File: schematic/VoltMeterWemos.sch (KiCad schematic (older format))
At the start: 22 parts, among them J1 TEST_1P, Q1 BS250, Q2 2N7000, SW1 SW_SPST, SW2 SW_SPST, U1 WeMosD1MiniPro

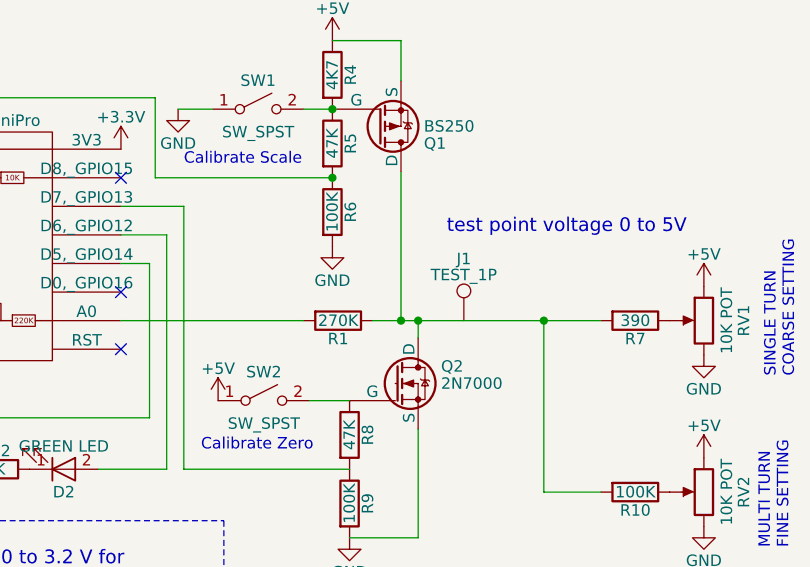
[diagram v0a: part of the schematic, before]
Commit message: capacitor added to A0
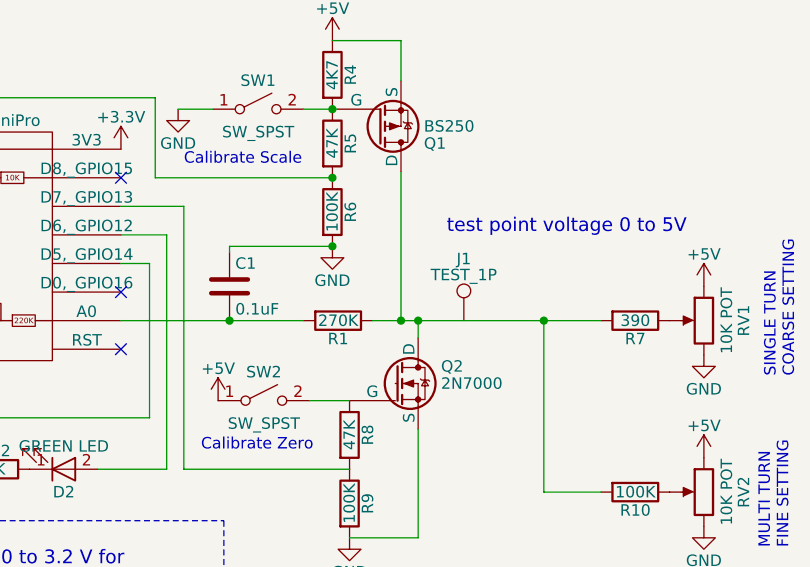
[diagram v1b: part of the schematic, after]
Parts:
- added C1: 0.1uF, symbol C
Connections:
- net GND: now also C1.1
- net at R1.2, U1.10 (A0): now also C1.2
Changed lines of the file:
@@
 NoConn ~ 4250 3450
 Wire Wire Line
-	5350 3325 5475 3325
-Wire Wire Line
-	5475 3325 5550 3325
-Wire Wire Line
-	5550 3325 6100 3325
-Wire Wire Line
-	6100 3325 6350 3325
+	5350 3325 6350 3325
 Text Notes 5675 2950 0    60   ~ 0
 test point voltage 0 to 5V
@@
 	1    0    0    -1
 $EndComp
+$Comp
+L C C1
+U 1 1 5A00E659
+P 4725 3175
+F 0 "C1" H 4750 3275 50  0000 L CNN
+F 1 "0.1uF" H 4750 3075 50  0000 L CNN
+F 2 "" H 4763 3025 50  0001 C CNN
+F 3 "" H 4725 3175 50  0001 C CNN
+	1    4725 3175
+	1    0    0    -1
+$EndComp
+Wire Wire Line
+	5175 3000 4725 3000
+Wire Wire Line
+	4725 3000 4725 3025
+Connection ~ 5175 3000
+Connection ~ 4725 3325
 $EndSCHEMATC

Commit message: lots of software and schematic updates, see diary for details. Moved results files to a private area since they are not of general interest.
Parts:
- Q1: value BS250 -> IR4905
- Q2: value 2N7000 -> IRFZ44N
- R7: value 390 -> 1000
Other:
- note added: "MULTI TURN\nCOARSE SETTING"
- note added: "SINGLE TURN\nFINE SETTING"
- note removed: "MULTI TURN\nFINE SETTING"
- note removed: "SINGLE TURN\nCOARSE SETTING"
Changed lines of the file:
@@
 P 5450 3600
 F 0 "Q2" H 5650 3675 50  0000 L CNN
-F 1 "2N7000" H 5650 3600 50  0000 L CNN
+F 1 "IRFZ44N" H 5650 3600 50  0000 L CNN
 F 2 "TO_SOT_Packages_THT:TO-92_Molded_Narrow" H 5650 3525 50  0001 L CIN
 F 3 "" H 5450 3600 50  0001 L CNN
@@
 P 5375 2475
 F 0 "Q1" H 5575 2550 50  0000 L CNN
-F 1 "BS250" H 5575 2475 50  0000 L CNN
+F 1 "IR4905" H 5575 2475 50  0000 L CNN
 F 2 "TO_SOT_Packages_THT:TO-92_Molded_Narrow" H 5575 2400 50  0001 L CIN
 F 3 "" H 5375 2475 50  0001 L CNN
@@
 P 6500 3325
 F 0 "R7" V 6580 3325 50  0000 C CNN
-F 1 "390" V 6500 3325 50  0000 C CNN
+F 1 "1000" V 6500 3325 50  0000 C CNN
 F 2 "" V 6430 3325 50  0001 C CNN
 F 3 "" H 6500 3325 50  0001 C CNN
@@
 Connection ~ 6100 3325
 Text Notes 7200 3575 1    50   ~ 0
-SINGLE TURN\nCOARSE SETTING
+MULTI TURN\nCOARSE SETTING
 Text Notes 7175 4325 1    50   ~ 0
-MULTI TURN\nFINE SETTING
+SINGLE TURN\nFINE SETTING
 Text Notes 4600 3900 0    50   ~ 0
 Calibrate Zero

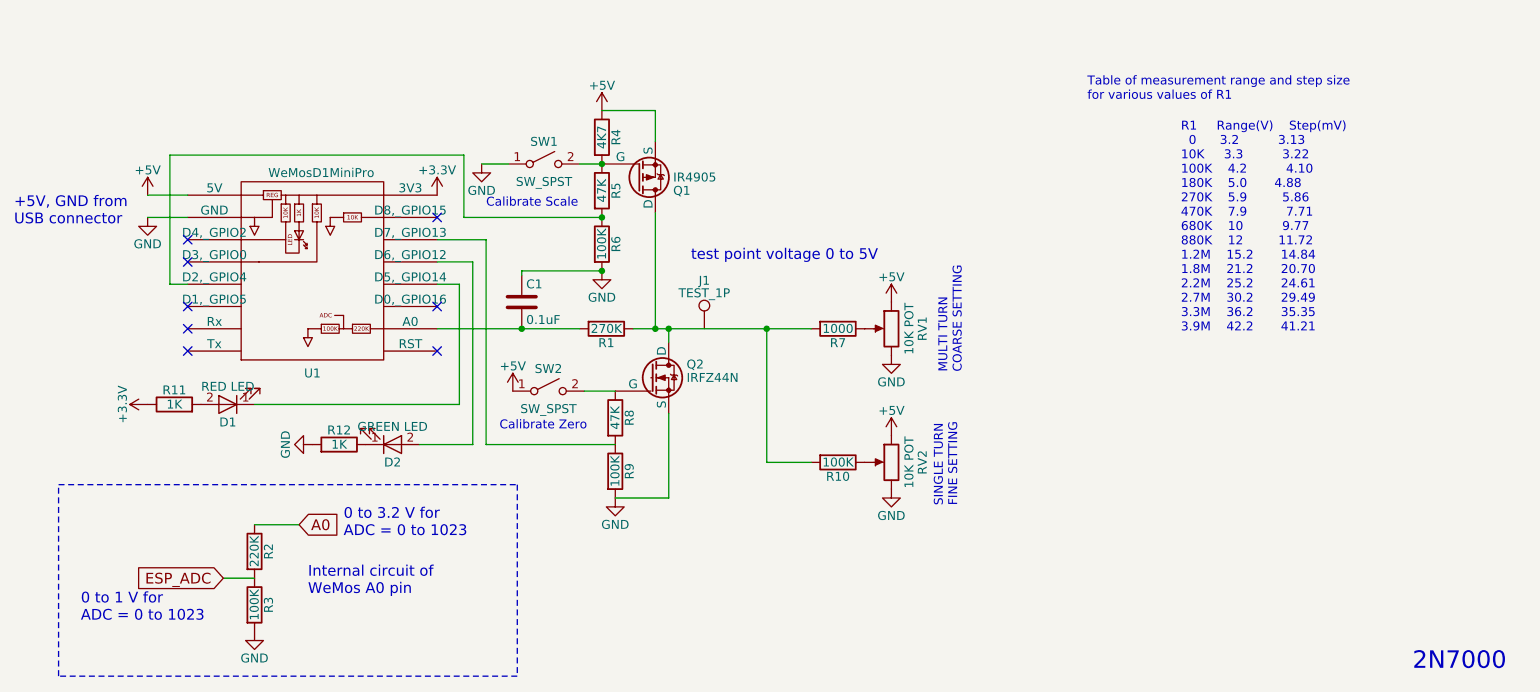
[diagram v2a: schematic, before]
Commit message: updates for pulse waveform on supply rail. See diary for more details
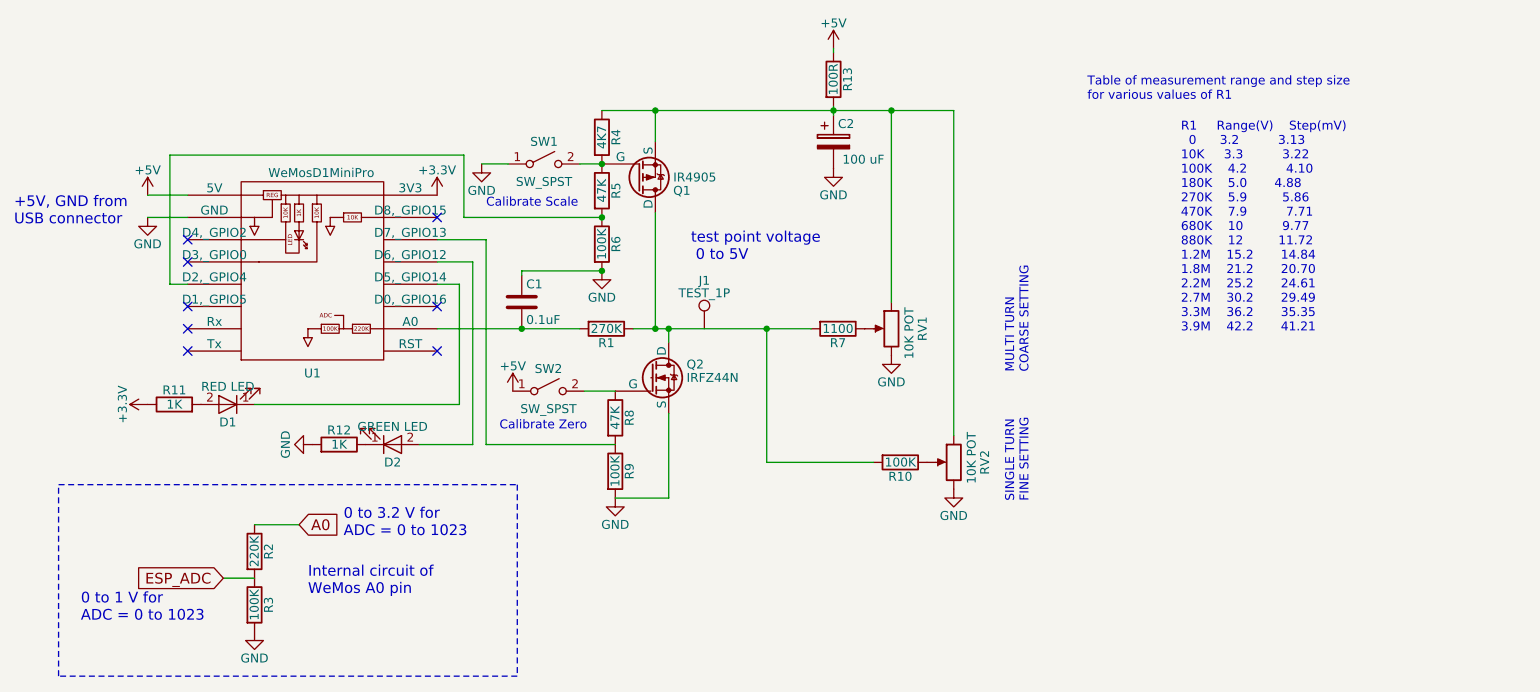
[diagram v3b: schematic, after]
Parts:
- added C2: 100 uF, symbol CP
- added R13: 100R, symbol R
- R7: value 1000 -> 1100
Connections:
- net +5V: now also R13.1; no longer Q1.3 (S), R4.1, RV1.1, RV2.1
- net GND: now also C2.2
- new net: C2.1, Q1.3 (S), R13.2, R4.1, RV1.1, RV2.1
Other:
- note added: "test point voltage\n 0 to 5V"
- note removed: "2N7000"
- note removed: "test point voltage 0 to 5V"
- moved on the sheet: R10, RV2
